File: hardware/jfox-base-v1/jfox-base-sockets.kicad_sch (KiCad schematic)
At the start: 3 parts, among them J1 Mezz A, J2 Mezz B, J3 Mezz C

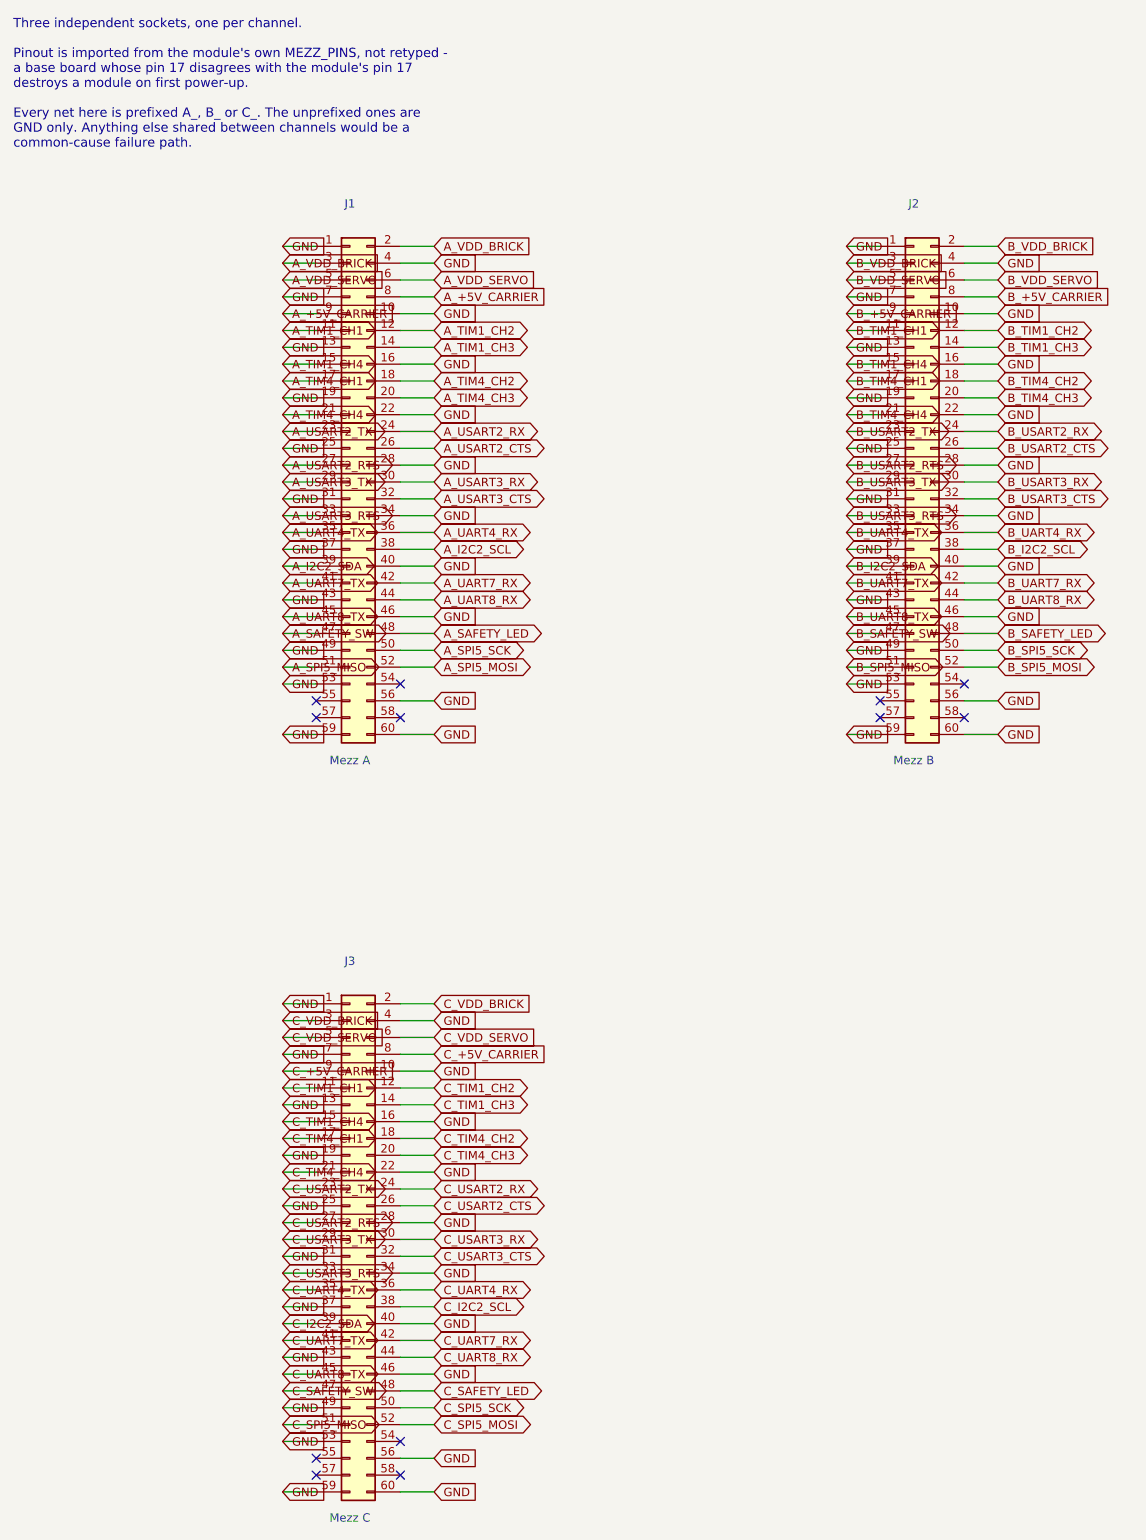
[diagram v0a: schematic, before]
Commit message: LTC4417 lands on the backplane, replacing the diode OR
It left the FCU when the power tree moved and never arrived here - the
backplane has been ORing its two airframe feeds with a pair of Schottkys,
which works and throws away the two things the part was chosen for:

  * Priority. A diode OR takes whichever feed is momentarily higher, so two
    supplies sitting 100 mV apart make the board chatter between them. The
    LTC4417 holds its selection until that source leaves its window.
  * A window. Under- and over-voltage per input, so a feed that has drifted
    out of spec is rejected rather than used because it is the higher of two
    bad ones.

It also drops ~0.4 V across a 5 V rail that the PMOS pass devices do not.

Two inputs, not three. V3 is tied to ground and its pass FET omitted, which
is how the datasheet says to leave an input out; inventing a third feed to
fill it would be worse. D50/D51 stay as reverse-polarity protection.

Three faults surfaced while wiring it, none of them the ORing:

  * The actuator headers still asked each channel for VDD_SERVO. That rail
    left the card's pinout when the power tree moved - servo power now runs
    from the backplane straight to the actuators and never passes through a
    card, which is the right way round. Three nets had nothing driving them.
  * EN was tied to +3V3, a rail the backplane does not have. It regulates
    nothing; the cards do. Now tied to the primary feed, so the part is
    enabled whenever there is power at all.
  * The expansion header overflowed. Its guard reported "25 spare signals
    will not fit a 20-pin header - widen it rather than dropping the
    overflow silently", which is exactly what it was written to catch. 2x15.

The far-face hole check earned itself again: a threshold divider placed on
the back landed under a card socket's through-holes. Bands on the back face
have to thread between sockets at y 20..27, 46..53 and 72..79.

  FCU        DRC 0 blocking, 105 parts, all checks pa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
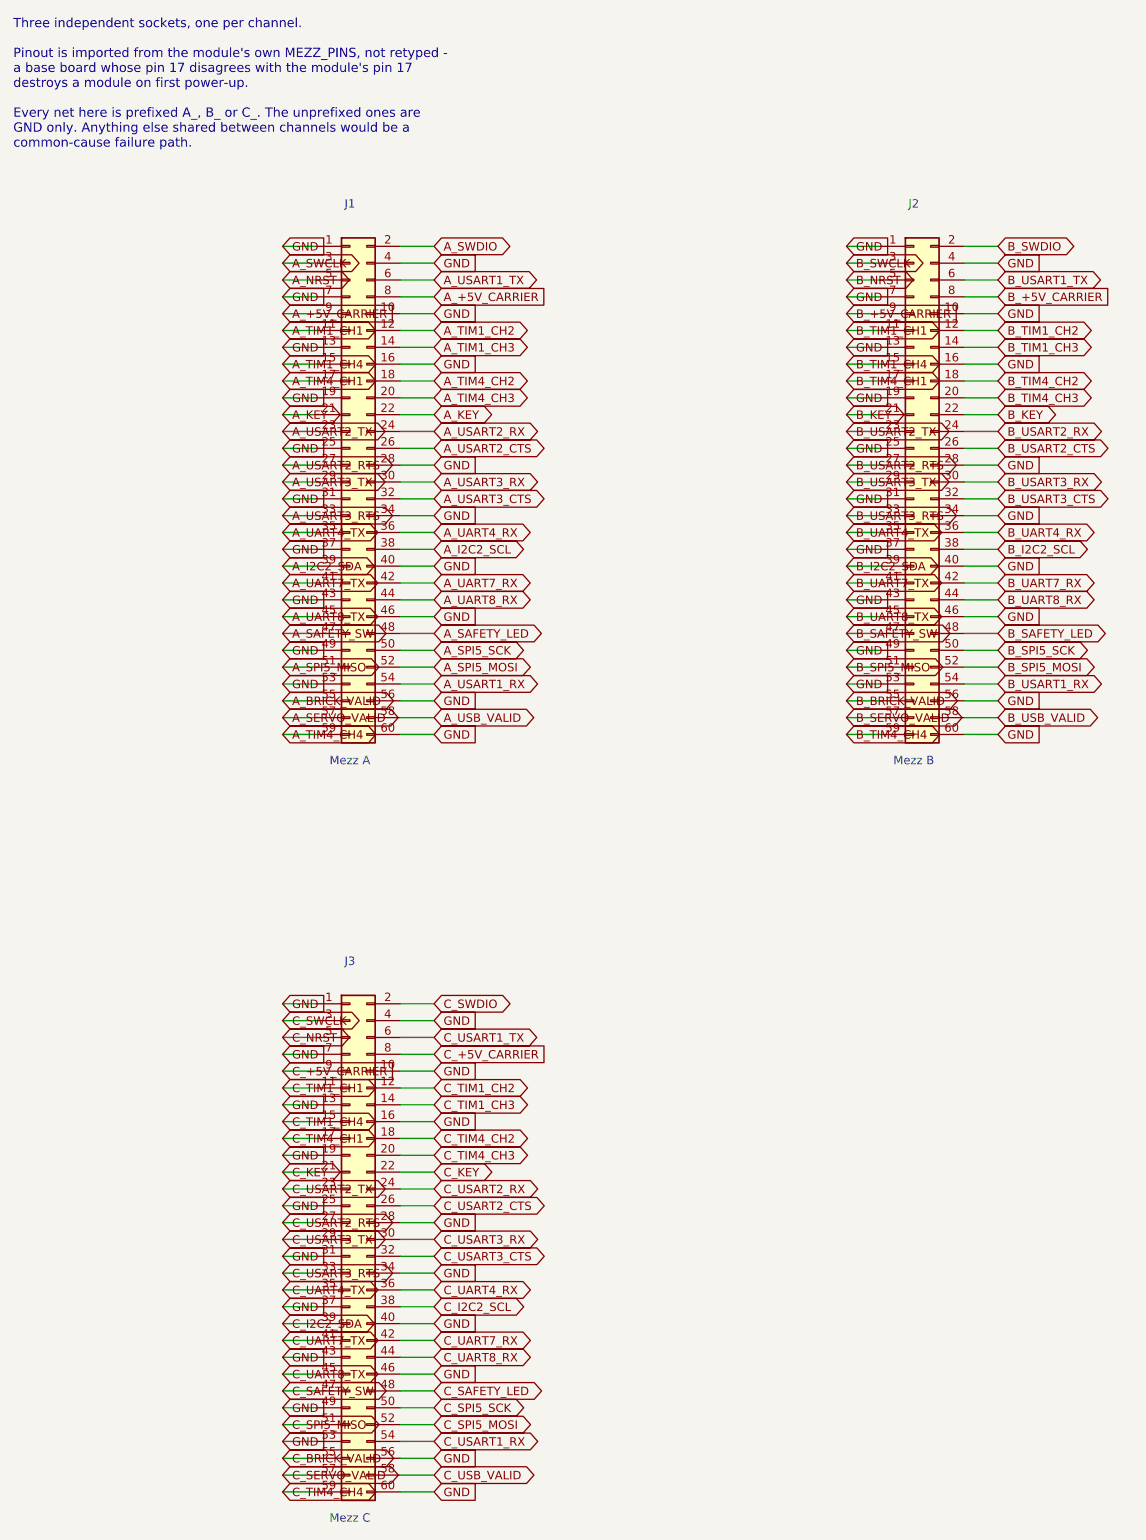
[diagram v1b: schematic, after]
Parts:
- J1, J2, J3: footprint Connector_PCBEdge:Samtec_MECF-30-01-NP-L-DV_2x30_P1.27mm_Socket_Horizontal -> Connector_PCBEdge:Samtec_MECF-30-01-L-DV_2x30_P1.27mm_Polarized_Socket_Horizontal
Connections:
- net A_TIM4_CH4: now also J1.59 (Pin_59); no longer J1.21 (Pin_21)
- net B_TIM4_CH4: now also J2.59 (Pin_59); no longer J2.21 (Pin_21)
- net C_TIM4_CH4: now also J3.59 (Pin_59); no longer J3.21 (Pin_21)
- net GND: no longer J1.22 (Pin_22), J1.59 (Pin_59), J2.22 (Pin_22), J2.59 (Pin_59), J3.22 (Pin_22), J3.59 (Pin_59)
- net B_USART1_RX: now reaches J2.54 (Pin_54)
- net B_BRICK_VALID: now reaches J2.55 (Pin_55)
- net B_SERVO_VALID: now reaches J2.57 (Pin_57)
- net B_USB_VALID: now reaches J2.58 (Pin_58)
- net A_USART1_RX: now reaches J1.54 (Pin_54)
- net A_BRICK_VALID: now reaches J1.55 (Pin_55)
- net A_SERVO_VALID: now reaches J1.57 (Pin_57)
- net A_USB_VALID: now reaches J1.58 (Pin_58)
- net C_USART1_RX: now reaches J3.54 (Pin_54)
- net C_BRICK_VALID: now reaches J3.55 (Pin_55)
- net C_SERVO_VALID: now reaches J3.57 (Pin_57)
- net C_USB_VALID: now reaches J3.58 (Pin_58)
- net A_VDD_BRICK renamed A_SWCLK
- net A_SWCLK: no longer J1.2 (Pin_2)
- net A_VDD_SERVO renamed A_NRST
- net A_NRST: no longer J1.6 (Pin_6)
- net B_VDD_BRICK renamed B_SWCLK
- net B_SWCLK: no longer J2.2 (Pin_2)
- net B_VDD_SERVO renamed B_NRST
- net B_NRST: no longer J2.6 (Pin_6)
- net C_VDD_BRICK renamed C_SWCLK
- net C_SWCLK: no longer J3.2 (Pin_2)
- net C_VDD_SERVO renamed C_NRST
- net C_NRST: no longer J3.6 (Pin_6)
- new net A_KEY: J1.21 (Pin_21), J1.22 (Pin_22)
- new net A_SWDIO: J1.2 (Pin_2)
- new net A_USART1_TX: J1.6 (Pin_6)
- new net B_KEY: J2.21 (Pin_21), J2.22 (Pin_22)
- new net B_SWDIO: J2.2 (Pin_2)
- new net B_USART1_TX: J2.6 (Pin_6)
- new net C_KEY: J3.21 (Pin_21), J3.22 (Pin_22)
- new net C_SWDIO: J3.2 (Pin_2)
- new net C_USART1_TX: J3.6 (Pin_6)
- no-connect marks 12 -> 0
